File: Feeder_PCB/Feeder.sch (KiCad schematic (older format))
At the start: 51 parts, among them P1 CONN_01X04, P2 CONN_01X08, P3 CONN_01X01, P4 CONN_01X08, P5 CONN_02X03, P6 CONN_01X04, P7 CONN_01X03, SW1 SW_PUSH, SW2 SW_PUSH, U1 STM32_mmvisual_JTAG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

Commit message: code als submodul hinzugefügt
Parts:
- removed P1: CONN_01X04, Connectors_JST:JST_XH_B04B-XH-A_04x2.50mm_Straight, symbol CONN_01X04
- added P1: CONN_01X05, Connectors_JST:JST_XH_B05B-XH-A_05x2.50mm_Straight, symbol CONN_01X05
- P3: footprint Pin_Headers:Pin_Header_Angled_1x01_Pitch2.54mm -> Pin_Headers:Pin_Header_Straight_1x01_Pitch2.54mm
- P7: footprint Pin_Headers:Pin_Header_Angled_1x03_Pitch2.54mm -> Pin_Headers:Pin_Header_Straight_1x03_Pitch2.54mm
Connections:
- net A: now also P1.1 (P1)
- net B: now also P1.4 (P4)
- net CAN_StandBy: now also U3.18 (CRS_SYNC/RCC_MCO/TIM1_CH1/USART1_CK/PA8); no longer U3.12 (ADC_IN6/I2S1_MCK/SPI1_MISO/TIM16_CH1/TIM1_BKIN/TIM3_CH1/TSC_G2_IO3/PA6)
- net MS1: now also U3.20 (I2C1_SDA/TIM17_BKIN/TIM1_CH3/TSC_G4_IO2/USART1_RX/PA10)
- net ~A: now also P1.2 (P2)
- net ~B: now also P1.3 (P3)
- net ~Enable: now also U3.19 (I2C1_SCL/TIM1_CH2/TSC_G4_IO1/USART1_TX/PA9); no longer U3.18 (CRS_SYNC/RCC_MCO/TIM1_CH1/USART1_CK/PA8)
- no-connect marks 4 -> 5
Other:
- moved on the sheet: C8, D2, D3, D4, D5, D6, D7, D8, D9, P2, P3, P4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

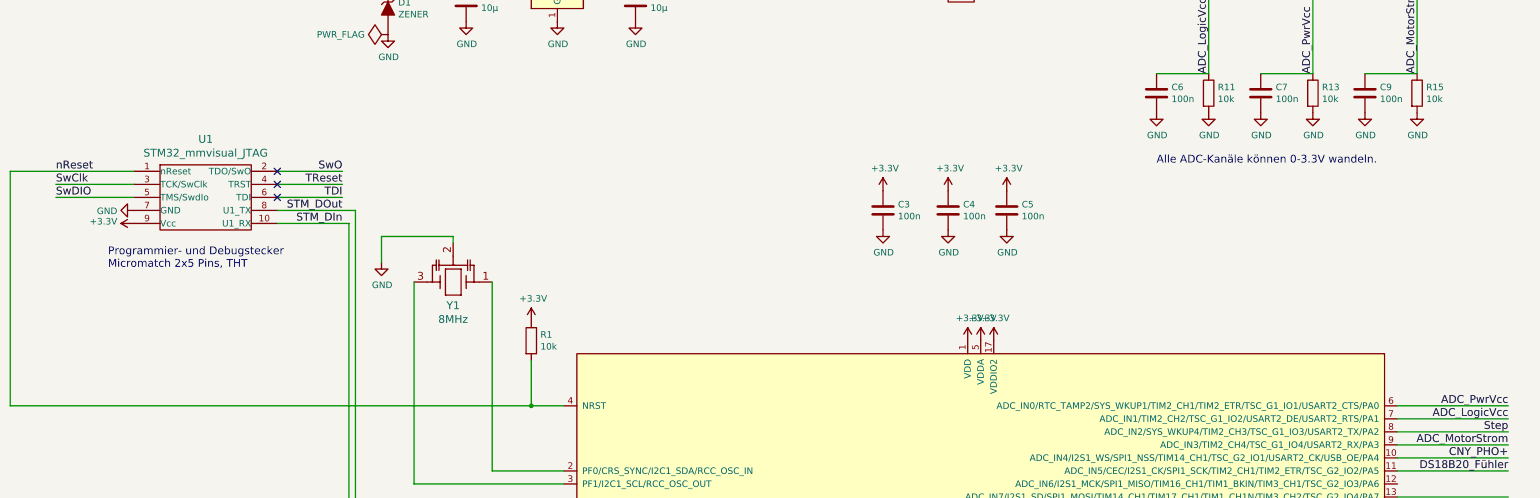
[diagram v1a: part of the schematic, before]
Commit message: neues Pr0jekt DomController hinzugefügt. Aktuell nur Schaltplan
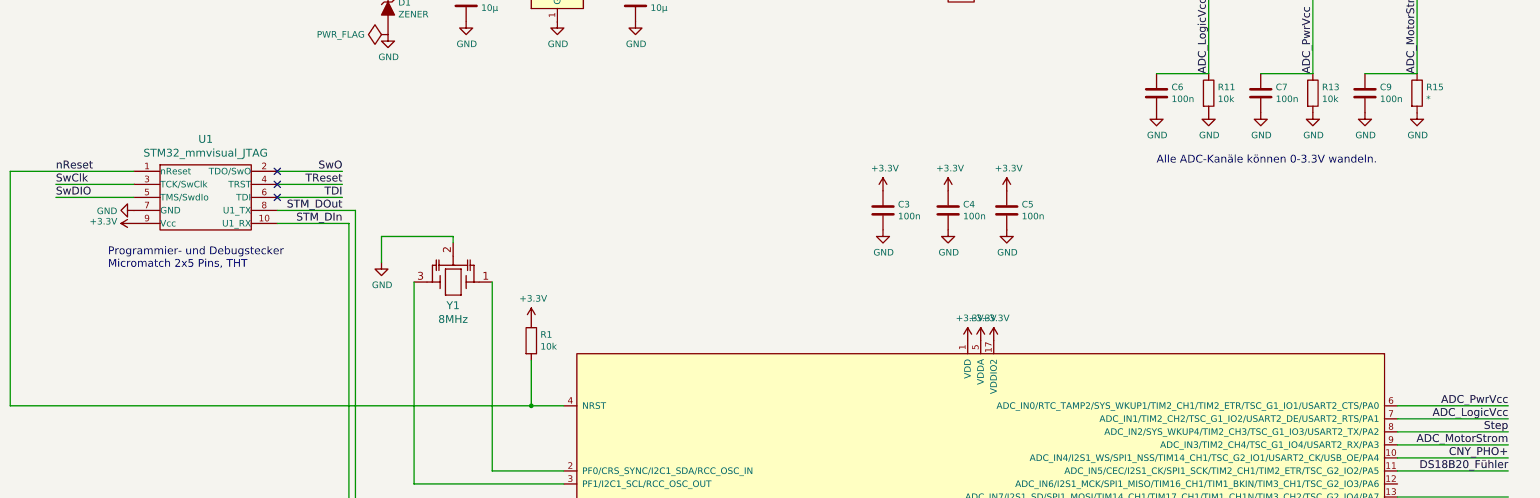
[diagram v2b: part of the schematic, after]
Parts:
- R15: value 10k -> *
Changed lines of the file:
@@
-EESchema Schematic File Version 2
-LIBS:power
-LIBS:device
-LIBS:transistors
-LIBS:conn
-LIBS:linear
-LIBS:regul
-LIBS:74xx
-LIBS:cmos4000
-LIBS:adc-dac
-LIBS:memory
-LIBS:xilinx
-LIBS:microcontrollers
-LIBS:dsp
-LIBS:microchip
-LIBS:analog_switches
-LIBS:motorola
-LIBS:texas
-LIBS:intel
-LIBS:audio
-LIBS:interface
-LIBS:digital-audio
-LIBS:philips
-LIBS:display
-LIBS:cypress
-LIBS:siliconi
-LIBS:opto
-LIBS:atmel
-LIBS:contrib
-LIBS:valves
-LIBS:stm32
-LIBS:Resonator_3pins
-LIBS:prog_sockets
-LIBS:ph-diodes
+EESchema Schematic File Version 4
 LIBS:Feeder-cache
-EELAYER 26 0
+EELAYER 29 0
 EELAYER END
 $Descr A3 16535 11693
@@
 $EndComp
 Wire Wire Line
-	700  4750 4950 4750
+	700  4750 4700 4750
 Wire Wire Line
 	700  4750 700  2950
@@
 P 11500 2350
 F 0 "R15" H 11570 2396 50  0000 L CNN
-F 1 "10k" H 11570 2305 50  0000 L CNN
+F 1 "*" H 11570 2305 50  0000 L CNN
 F 2 "Resistors_SMD:R_0603" V 6080 -1600 50  0001 C CNN
 F 3 "" H 6150 -1600 50  0000 C CNN
@@
 Wire Wire Line
 	1800 8850 1900 8850
+Wire Wire Line
+	4700 4750 4950 4750
 $EndSCHEMATC
